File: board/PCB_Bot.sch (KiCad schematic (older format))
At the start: 18 parts, among them J1 Screw_Terminal_01x04, J2 Conn_02x15_Top_Bottom, J3 Conn_02x15_Top_Bottom, J4 Screw_Terminal_01x02, J5 Screw_Terminal_01x03, U1 TB6612FNG, U2 LSM9DS1

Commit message: update pcbnew orienatation
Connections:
- net RST: no longer J3.5 (Pin_5), J3.6 (Pin_6)
- new net RST1: J3.5 (Pin_5), J3.6 (Pin_6)
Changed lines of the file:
@@
 GND
 Text GLabel 9900 1750 0    50   Input ~ 0
-RST
+RST1
 Text GLabel 9850 1850 0    50   Input ~ 0
 5V
@@
 Connection ~ 3300 750
 Wire Wire Line
-	3300 750  3900 750
+	3300 750  3600 750
 Wire Wire Line
 	3300 1150 3300 1250
@@
 Wire Wire Line
 	7000 2950 7250 2950
+$Comp
+L power:PWR_FLAG #FLG?
+U 1 1 5E56B89A
+P 3600 750
+F 0 "#FLG?" H 3600 825 50  0001 C CNN
+F 1 "PWR_FLAG" H 3600 923 50  0000 C CNN
+F 2 "" H 3600 750 50  0001 C CNN
+F 3 "~" H 3600 750 50  0001 C CNN
+	1    3600 750
+	1    0    0    -1
+$EndComp
+Connection ~ 3600 750
+Wire Wire Line
+	3600 750  3900 750
 $EndSCHEMATC

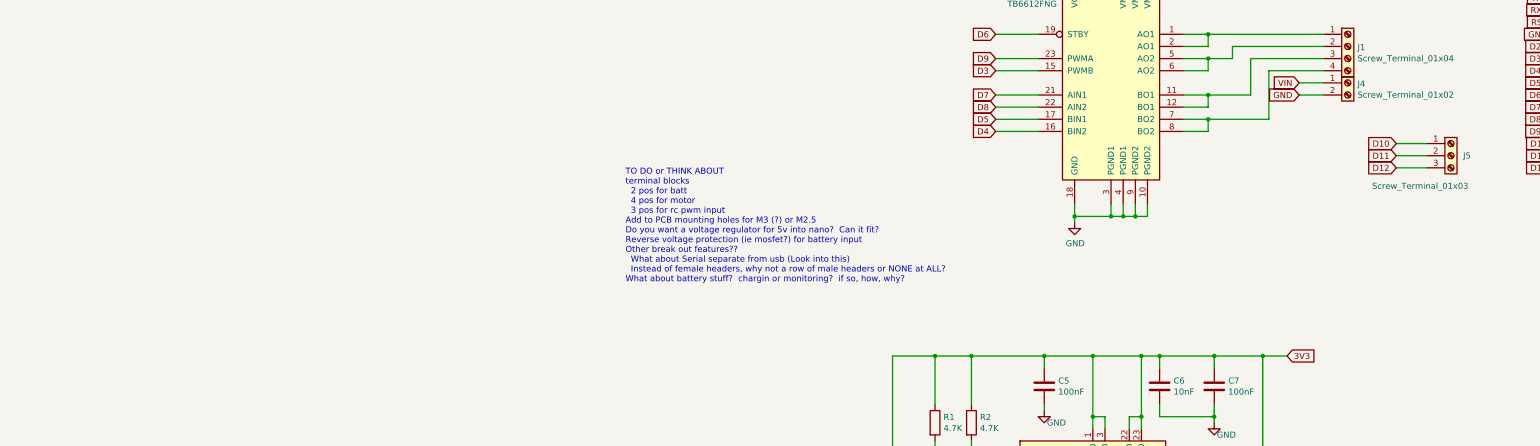
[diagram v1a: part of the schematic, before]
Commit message: update pcbnew and add some tracks - that can be replaced at some point...
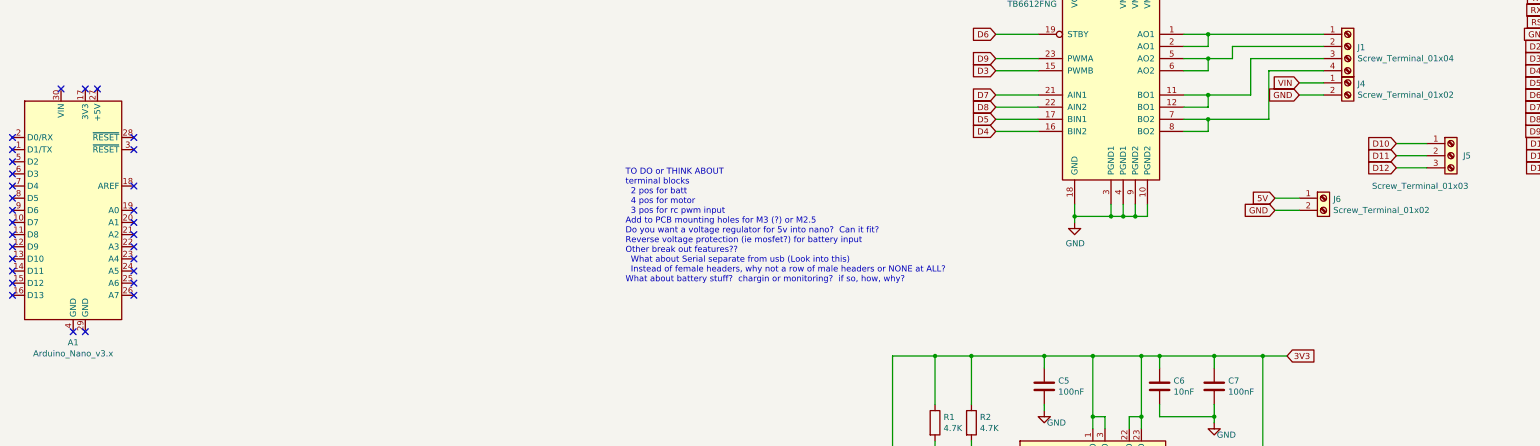
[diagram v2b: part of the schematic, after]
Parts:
- added A1: Arduino_Nano_v3.x, Module:Arduino_Nano, symbol MCU_Module:Arduino_Nano_v3.x
- added J6: Screw_Terminal_01x02, Connector_Phoenix_MC:PhoenixContact_MCV_1,5_2-G-3.5_1x02_P3.50mm_Vertical, symbol Connector:Screw_Terminal_01x02
- C1, C3: footprint Capacitor_SMD:C_0603_1608Metric -> Capacitor_SMD:C_01005_0402Metric
- C2, C4: footprint Capacitor_SMD:C_0805_2012Metric -> Capacitor_SMD:C_0201_0603Metric
- C5, C7, C9: footprint Capacitor_SMD:C_0805_2012Metric -> Capacitor_SMD:C_01005_0402Metric
- C6, C8: footprint Capacitor_SMD:C_0603_1608Metric -> Capacitor_SMD:C_0201_0603Metric
- R1, R2: footprint Resistor_SMD:R_0603_1608Metric -> Resistor_SMD:R_01005_0402Metric
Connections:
- net +5V: now also J6.1 (Pin_1)
- net GND: now also J6.2 (Pin_2)
- no-connect marks 5 -> 35
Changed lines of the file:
@@
 F 0 "C3" H 5365 1046 50  0000 L CNN
 F 1 "0.1uF" H 5365 955 50  0000 L CNN
-F 2 "Capacitor_SMD:C_0603_1608Metric" H 5288 850 50  0001 C CNN
+F 2 "Capacitor_SMD:C_01005_0402Metric" H 5288 850 50  0001 C CNN
 F 3 "~" H 5250 1000 50  0001 C CNN
 	1    5250 1000
@@
 F 0 "C1" H 3415 1046 50  0000 L CNN
 F 1 "0.1uF" H 3415 955 50  0000 L CNN
-F 2 "Capacitor_SMD:C_0603_1608Metric" H 3338 850 50  0001 C CNN
+F 2 "Capacitor_SMD:C_01005_0402Metric" H 3338 850 50  0001 C CNN
 F 3 "~" H 3300 1000 50  0001 C CNN
 	1    3300 1000
@@
 F 0 "C4" H 5865 1046 50  0000 L CNN
 F 1 "10uF" H 5865 955 50  0000 L CNN
-F 2 "Capacitor_SMD:C_0805_2012Metric" H 5750 1000 50  0001 C CNN
+F 2 "Capacitor_SMD:C_0201_0603Metric" H 5750 1000 50  0001 C CNN
 F 3 "~" H 5750 1000 50  0001 C CNN
 	1    5750 1000
@@
 F 0 "C2" H 4015 1046 50  0000 L CNN
 F 1 "10uF" H 4015 955 50  0000 L CNN
-F 2 "Capacitor_SMD:C_0805_2012Metric" H 3900 1000 50  0001 C CNN
+F 2 "Capacitor_SMD:C_0201_0603Metric" H 3900 1000 50  0001 C CNN
 F 3 "~" H 3900 1000 50  0001 C CNN
 	1    3900 1000
@@
 F 0 "C9" H 3665 6746 50  0000 L CNN
 F 1 "100nF" H 3665 6655 50  0000 L CNN
-F 2 "Capacitor_SMD:C_0805_2012Metric" H 3588 6550 50  0001 C CNN
+F 2 "Capacitor_SMD:C_01005_0402Metric" H 3588 6550 50  0001 C CNN
 F 3 "~" H 3550 6700 50  0001 C CNN
 	1    3550 6700
@@
 F 0 "C8" H 3215 6746 50  0000 L CNN
 F 1 "10nF" H 3215 6655 50  0000 L CNN
-F 2 "Capacitor_SMD:C_0603_1608Metric" H 3138 6550 50  0001 C CNN
+F 2 "Capacitor_SMD:C_0201_0603Metric" H 3138 6550 50  0001 C CNN
 F 3 "~" H 3100 6700 50  0001 C CNN
 	1    3100 6700
@@
 F 0 "C6" H 5165 4796 50  0000 L CNN
 F 1 "10nF" H 5165 4705 50  0000 L CNN
-F 2 "Capacitor_SMD:C_0603_1608Metric" H 5088 4600 50  0001 C CNN
+F 2 "Capacitor_SMD:C_0201_0603Metric" H 5088 4600 50  0001 C CNN
 F 3 "~" H 5050 4750 50  0001 C CNN
 	1    5050 4750
@@
 F 0 "C7" H 5615 4796 50  0000 L CNN
 F 1 "100nF" H 5615 4705 50  0000 L CNN
-F 2 "Capacitor_SMD:C_0805_2012Metric" H 5538 4600 50  0001 C CNN
+F 2 "Capacitor_SMD:C_01005_0402Metric" H 5538 4600 50  0001 C CNN
 F 3 "~" H 5500 4750 50  0001 C CNN
 	1    5500 4750
@@
 F 0 "C5" H 4215 4796 50  0000 L CNN
 F 1 "100nF" H 4215 4705 50  0000 L CNN
-F 2 "Capacitor_SMD:C_0805_2012Metric" H 4138 4600 50  0001 C CNN
+F 2 "Capacitor_SMD:C_01005_0402Metric" H 4138 4600 50  0001 C CNN
 F 3 "~" H 4100 4750 50  0001 C CNN
 	1    4100 4750
@@
 F 0 "R2" H 3570 5096 50  0000 L CNN
 F 1 "4.7K" H 3570 5005 50  0000 L CNN
-F 2 "Resistor_SMD:R_0603_1608Metric" V 3430 5050 50  0001 C CNN
+F 2 "Resistor_SMD:R_01005_0402Metric" V 3430 5050 50  0001 C CNN
 F 3 "~" H 3500 5050 50  0001 C CNN
 	1    3500 5050
@@
 F 0 "R1" H 3270 5096 50  0000 L CNN
 F 1 "4.7K" H 3270 5005 50  0000 L CNN
-F 2 "Resistor_SMD:R_0603_1608Metric" V 3130 5050 50  0001 C CNN
+F 2 "Resistor_SMD:R_01005_0402Metric" V 3130 5050 50  0001 C CNN
 F 3 "~" H 3200 5050 50  0001 C CNN
 	1    3200 5050
@@
 	7000 2950 7250 2950
 $Comp
-L power:PWR_FLAG #FLG?
+L power:PWR_FLAG #FLG0101
 U 1 1 5E56B89A
 P 3600 750
-F 0 "#FLG?" H 3600 825 50  0001 C CNN
+F 0 "#FLG0101" H 3600 825 50  0001 C CNN
 F 1 "PWR_FLAG" H 3600 923 50  0000 C CNN
 F 2 "" H 3600 750 50  0001 C CNN
@@
 Wire Wire Line
 	3600 750  3900 750
+$Comp
+L Connector:Screw_Terminal_01x02 J6
+U 1 1 5E5C9A80
+P 6400 3200
+F 0 "J6" H 6480 3192 50  0000 L CNN
+F 1 "Screw_Terminal_01x02" H 6480 3101 50  0000 L CNN
+F 2 "Connector_Phoenix_MC:PhoenixContact_MCV_1,5_2-G-3.5_1x02_P3.50mm_Vertical" H 6400 3200 50  0001 C CNN
+F 3 "~" H 6400 3200 50  0001 C CNN
+	1    6400 3200
+	1    0    0    -1
+$EndComp
+Text GLabel 6000 3300 0    50   Input ~ 0
+GND
+Text GLabel 6000 3200 0    50   Input ~ 0
+5V
+Wire Wire Line
+	6000 3200 6200 3200
+Wire Wire Line
+	6200 3300 6000 3300
+$Comp
+L MCU_Module:Arduino_Nano_v3.x A1
+U 1 1 5E5F3EC8
+P -3900 3300
+F 0 "A1" H -3900 2211 50  0000 C CNN
+F 1 "Arduino_Nano_v3.x" H -3900 2120 50  0000 C CNN
+F 2 "Module:Arduino_Nano" H -3900 3300 50  0001 C CIN
+F 3 "http://www.mouser.com/pdfdocs/Gravitech_Arduino_Nano3_0.pdf" H -3900 3300 50  0001 C CNN
+	1    -3900 3300
+	1    0    0    -1
+$EndComp
+NoConn ~ -4000 2300
+NoConn ~ -3800 2300
+NoConn ~ -3700 2300
+NoConn ~ -3400 2700
+NoConn ~ -3400 2800
+NoConn ~ -3400 3100
+NoConn ~ -3400 3300
+NoConn ~ -3400 3400
+NoConn ~ -3400 3500
+NoConn ~ -3400 3600
+NoConn ~ -3400 3700
+NoConn ~ -3400 3800
+NoConn ~ -3400 3900
+NoConn ~ -3400 4000
+NoConn ~ -3800 4300
+NoConn ~ -3900 4300
+NoConn ~ -4400 4000
+NoConn ~ -4400 3900
+NoConn ~ -4400 3800
+NoConn ~ -4400 3700
+NoConn ~ -4400 3600
+NoConn ~ -4400 3500
+NoConn ~ -4400 3400
+NoConn ~ -4400 3300
+NoConn ~ -4400 3200
+NoConn ~ -4400 3100
+NoConn ~ -4400 3000
+NoConn ~ -4400 2900
+NoConn ~ -4400 2800
+NoConn ~ -4400 2700
 $EndSCHEMATC

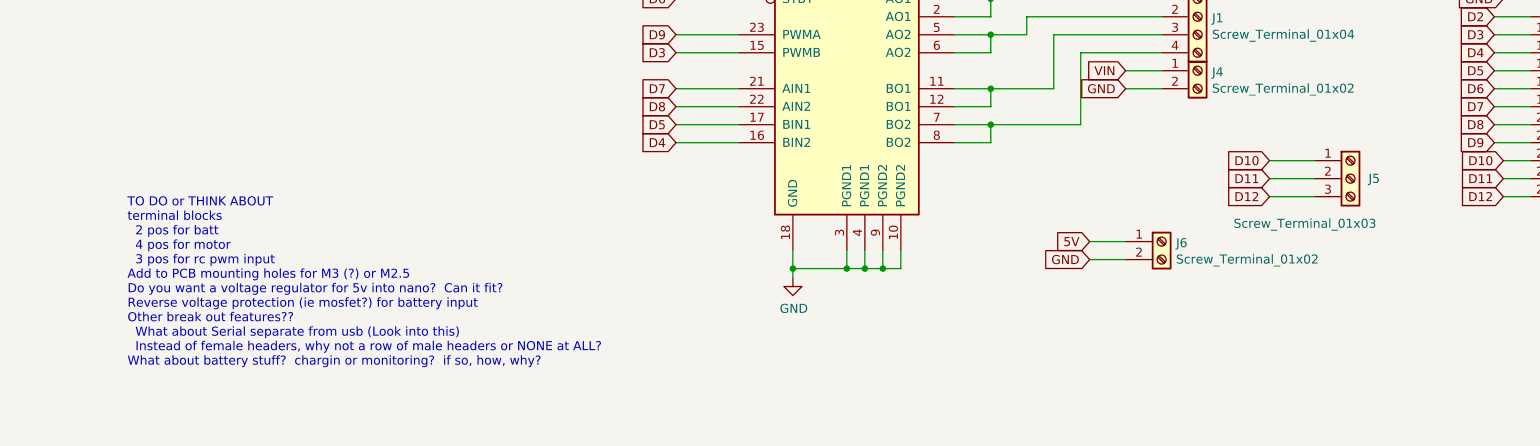
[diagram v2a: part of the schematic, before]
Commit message: look at layout of nano, add notes_examples to md files
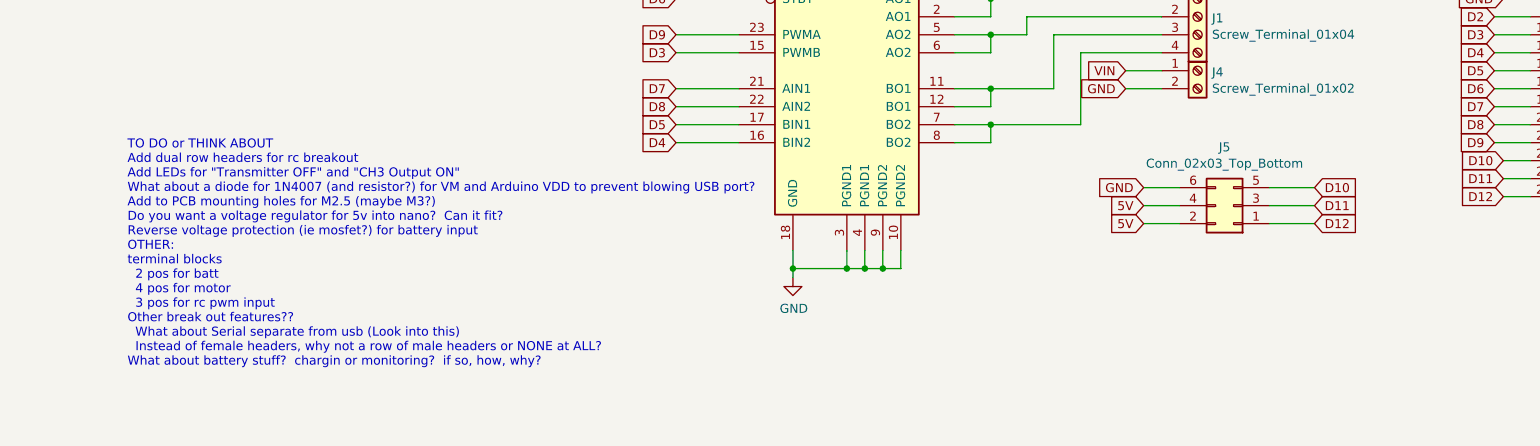
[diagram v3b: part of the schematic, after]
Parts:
- removed J5: Screw_Terminal_01x03, Connector_Phoenix_MC:PhoenixContact_MCV_1,5_3-G-3.5_1x03_P3.50mm_Vertical, symbol Connector:Screw_Terminal_01x03
- removed J6: Screw_Terminal_01x02, Connector_Phoenix_MC:PhoenixContact_MCV_1,5_2-G-3.5_1x02_P3.50mm_Vertical, symbol Connector:Screw_Terminal_01x02
- added J5: Conn_02x03_Top_Bottom, Connector_PinHeader_2.54mm:PinHeader_2x03_P2.54mm_Horizontal, symbol Connector_Generic:Conn_02x03_Odd_Even
- J1: footprint Connector_Phoenix_MC:PhoenixContact_MCV_1,5_4-G-3.5_1x04_P3.50mm_Vertical -> Rnanobot:PTSM_Phoenix_Contact_4-pos_Base_Strip_1815280
- J4: footprint Connector_Phoenix_MC:PhoenixContact_MCV_1,5_2-G-3.5_1x02_P3.50mm_Vertical -> Rnanobot:PTSM_Phoenix_Contact_2-pos_Base_Strip_1815264
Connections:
- net +5V: now also J5.2 (Pin_2), J5.4 (Pin_4)
- net D10: now also J5.5 (Pin_5)
- net D11: now also J5.3 (Pin_3)
- net D12: now also J5.1 (Pin_1)
- net GND: now also J5.6 (Pin_6)
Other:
- note added: "TO DO or THINK ABOUT\nAdd dual row headers for rc breakout\nAdd LEDs for "Transmitter OFF" and "CH3 Output ON"\nWhat about a diode for 1N4007 (and resistor?) for VM and Arduino VDD to prevent blowing USB port?\nAdd to PCB mounting holes for M2.5 (maybe M3?)\nDo you want a voltage regulator for 5v into nano? Can it fit?\nReverse voltage protection (ie mosfet?) for battery input\nOTHER:\nterminal b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"
- note removed: "TO DO or THINK ABOUT\nterminal blocks\n 2 pos for batt\n 4 pos for motor\n 3 pos for rc pwm input\nAdd to PCB mounting holes for M3 (?) or M2.5\nDo you want a voltage regulator for 5v into nano? Can it fit?\nReverse voltage protection (ie mosfet?) for battery input\nOther break out features??\n What about Serial separate from usb (Look into this)\n Instead of female headers, why not a row of male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"
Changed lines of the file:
@@
 3V3
 Text Notes 650  3900 0    50   ~ 0
-TO DO or THINK ABOUT\nterminal blocks\n  2 pos for batt\n  4 pos for motor\n  3 pos for rc pwm input\nAdd to PCB mounting holes for M3 (?) or M2.5\nDo you want a voltage regulator for 5v into nano?  Can it fit?\nReverse voltage protection (ie mosfet?) for battery input\nOther break out features??\n  What about Serial separate from usb (Look into this)\n  Instead of female headers, why not a row of male headers or NONE at ALL?  \nWhat about battery stuff?  chargin or monitoring?  if so, how, why?\n
+TO DO or THINK ABOUT\nAdd dual row headers for rc breakout\nAdd LEDs for "Transmitter OFF" and "CH3 Output ON"\nWhat about a diode for 1N4007 (and resistor?) for VM and Arduino VDD to prevent blowing USB port?\nAdd to PCB mounting holes for M2.5 (maybe M3?)\nDo you want a voltage regulator for 5v into nano?  Can it fit?\nReverse voltage protection (ie mosfet?) for battery input\nOTHER:\nterminal blocks\n  2 pos for batt\n  4 pos for motor\n  3 pos for rc pwm input\nOther break out features??\n  What about Serial separate from usb (Look into this)\n  Instead of female headers, why not a row of male headers or NONE at ALL?  \nWhat about battery stuff?  chargin or monitoring?  if so, how, why?\n
 $Comp
 L power:+7.5V #PWR01
@@
 F 0 "J4" H 6680 2242 50  0000 L CNN
 F 1 "Screw_Terminal_01x02" H 6680 2151 50  0000 L CNN
-F 2 "Connector_Phoenix_MC:PhoenixContact_MCV_1,5_2-G-3.5_1x02_P3.50mm_Vertical" H 6600 2250 50  0001 C CNN
+F 2 "Rnanobot:PTSM_Phoenix_Contact_2-pos_Base_Strip_1815264" H 6600 2250 50  0001 C CNN
 F 3 "~" H 6600 2250 50  0001 C CNN
 	1    6600 2250
@@
 F 0 "J1" H 6680 1942 50  0000 L CNN
 F 1 "Screw_Terminal_01x04" H 6680 1851 50  0000 L CNN
-F 2 "Connector_Phoenix_MC:PhoenixContact_MCV_1,5_4-G-3.5_1x04_P3.50mm_Vertical" H 6600 1950 50  0001 C CNN
+F 2 "Rnanobot:PTSM_Phoenix_Contact_4-pos_Base_Strip_1815280" H 6600 1950 50  0001 C CNN
 F 3 "~" H 6600 1950 50  0001 C CNN
 	1    6600 1950
 	1    0    0    -1
 $EndComp
-$Comp
-L Connector:Screw_Terminal_01x03 J5
-U 1 1 5E55855D
-P 7450 2850
-F 0 "J5" H 7550 2850 50  0000 L CNN
-F 1 "Screw_Terminal_01x03" H 6800 2600 50  0000 L CNN
-F 2 "Connector_Phoenix_MC:PhoenixContact_MCV_1,5_3-G-3.5_1x03_P3.50mm_Vertical" H 7450 2850 50  0001 C CNN
-F 3 "~" H 7450 2850 50  0001 C CNN
-	1    7450 2850
-	1    0    0    -1
-$EndComp
-Text GLabel 7000 2750 0    50   Input ~ 0
+Text GLabel 7250 2900 2    50   Input ~ 0
 D10
-Text GLabel 7000 2850 0    50   Input ~ 0
+Text GLabel 7250 3000 2    50   Input ~ 0
 D11
-Text GLabel 7000 2950 0    50   Input ~ 0
+Text GLabel 7250 3100 2    50   Input ~ 0
 D12
-Wire Wire Line
-	7000 2750 7250 2750
-Wire Wire Line
-	7250 2850 7000 2850
-Wire Wire Line
-	7000 2950 7250 2950
 $Comp
 L power:PWR_FLAG #FLG0101
@@
 Wire Wire Line
 	3600 750  3900 750
-$Comp
-L Connector:Screw_Terminal_01x02 J6
-U 1 1 5E5C9A80
-P 6400 3200
-F 0 "J6" H 6480 3192 50  0000 L CNN
-F 1 "Screw_Terminal_01x02" H 6480 3101 50  0000 L CNN
-F 2 "Connector_Phoenix_MC:PhoenixContact_MCV_1,5_2-G-3.5_1x02_P3.50mm_Vertical" H 6400 3200 50  0001 C CNN
-F 3 "~" H 6400 3200 50  0001 C CNN
-	1    6400 3200
-	1    0    0    -1
-$EndComp
-Text GLabel 6000 3300 0    50   Input ~ 0
+Text GLabel 6300 2900 0    50   Input ~ 0
 GND
-Text GLabel 6000 3200 0    50   Input ~ 0
+Text GLabel 6300 3100 0    50   Input ~ 0
 5V
-Wire Wire Line
-	6000 3200 6200 3200
-Wire Wire Line
-	6200 3300 6000 3300
 $Comp
 L MCU_Module:Arduino_Nano_v3.x A1
@@
 NoConn ~ -4400 2800
 NoConn ~ -4400 2700
+Text GLabel 6300 3000 0    50   Input ~ 0
+5V
+$Comp
+L Connector_Generic:Conn_02x03_Odd_Even J5
+U 1 1 5E5C549C
+P 6800 3000
+F 0 "J5" H 6850 2675 50  0000 C CNN
+F 1 "Conn_02x03_Top_Bottom" H 6850 2766 50  0000 C CNN
+F 2 "Connector_PinHeader_2.54mm:PinHeader_2x03_P2.54mm_Horizontal" H 6800 3000 50  0001 C CNN
+F 3 "~" H 6800 3000 50  0001 C CNN
+	1    6800 3000
+	-1   0    0    1
+$EndComp
+Wire Wire Line
+	7000 2900 7250 2900
+Wire Wire Line
+	7000 3000 7250 3000
+Wire Wire Line
+	7000 3100 7250 3100
+Wire Wire Line
+	6500 2900 6300 2900
+Wire Wire Line
+	6500 3000 6300 3000
+Wire Wire Line
+	6500 3100 6300 3100
 $EndSCHEMATC
